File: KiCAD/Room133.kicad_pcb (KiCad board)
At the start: 4 copper layers, 47.6 x 39.4 mm, 39 parts, among them J1 Edge2x6_Connector, J2 USB_B_Micro, U1 ESP32-WROOM-32, U2 AMS1117-3.3, U3 SHTC3

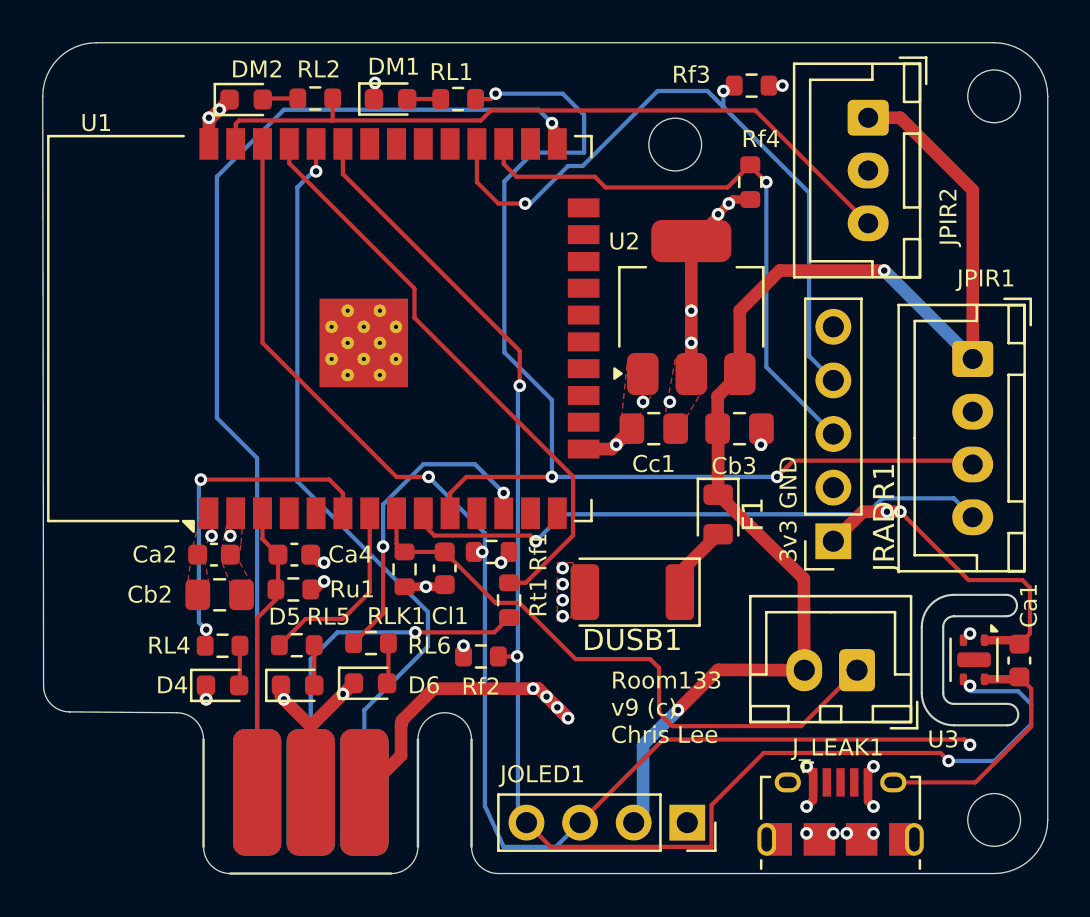
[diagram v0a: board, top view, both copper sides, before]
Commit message: Updates for v10 Room133 board (#13)
- Update KiCad design
- SHTC3 has better thermal isolation.  Ebox updated for its new position.
- Fixed library for edge footprint
- Two LEDs were driven using input-only pins (gpio34,gpio35), so moved to gpio18, gpio19.
- Updated to KiCAD 8.0 format
- Documentation for PIR wire.
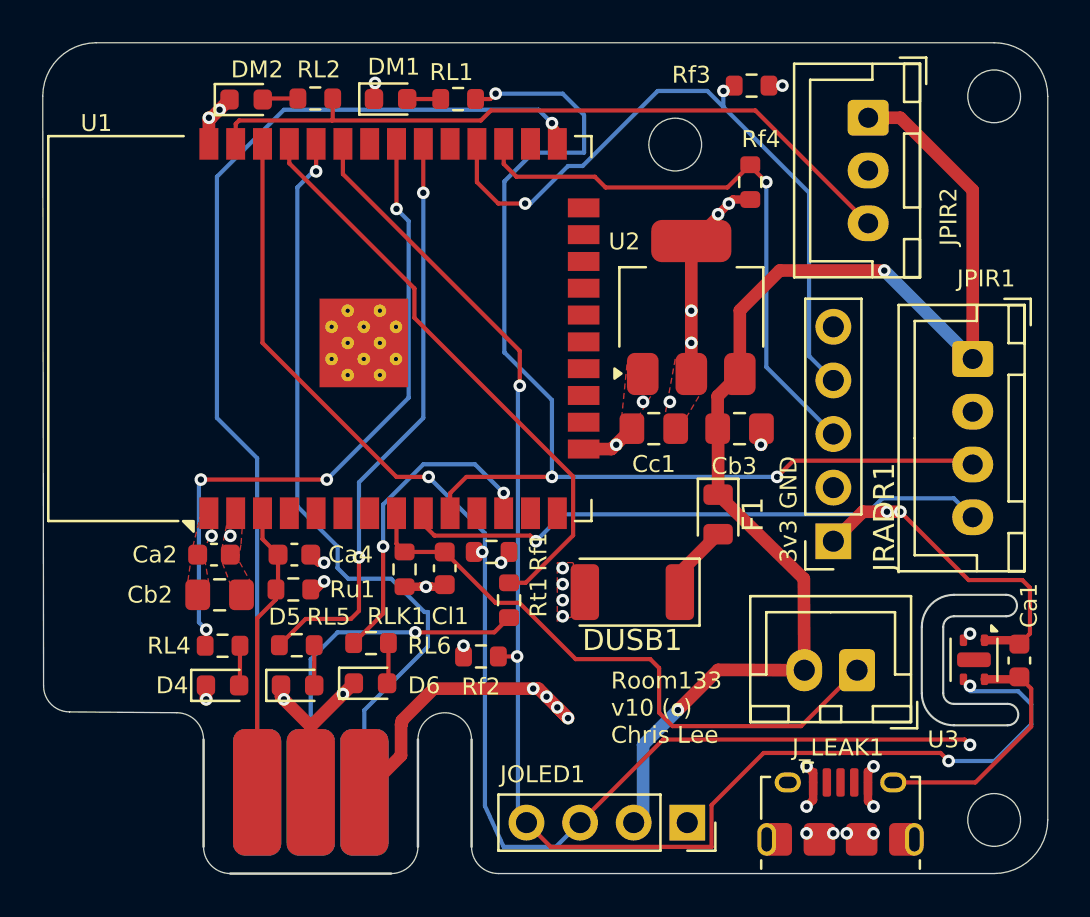
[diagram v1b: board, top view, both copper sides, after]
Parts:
- J1: footprint Library:EdgeConnectorA_2x3 -> chl33_library:EdgeConnectorA_2x3
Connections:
- U1 pad 30: unconnected-(U1-IO18-Pad30) -> LED2
- U1 pad 31: unconnected-(U1-IO19-Pad31) -> LED1
- U1 pad 6: LED1 -> unconnected-(U1-IO34-Pad6)
- U1 pad 7: LED2 -> unconnected-(U1-IO35-Pad7)
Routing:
- net LED2: track 9.06 -> 27.8 mm, vias 0 -> 2
- net LED1: track 16.0 -> 31.9 mm, vias 2 -> 4
- net TXC: track 35.0 -> 36.3 mm
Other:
- board text added: "Room133 v10 (c) Chris Lee"
- board text removed: "Room133 v9 (c) Chris Lee"
